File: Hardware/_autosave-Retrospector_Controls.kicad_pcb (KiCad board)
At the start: 2 copper layers, 60 x 110 mm, 32 parts, among them J1 Conn_01x08_Female, J10 Feedback_CV, J11 Audio_In_R, J12 Audio_Out_R, J13 Audio_Out_L, J14 Filter, J2 Conn_01x08_Female, J3 Conn_01x08_Female, J4 Conn_01x08_Female, J5 Audio_In_L, J6 Delay_CV_L, J7 Mix_CV, J8 Delay_CV_R, J9 Clock, U1 TB62781FNG

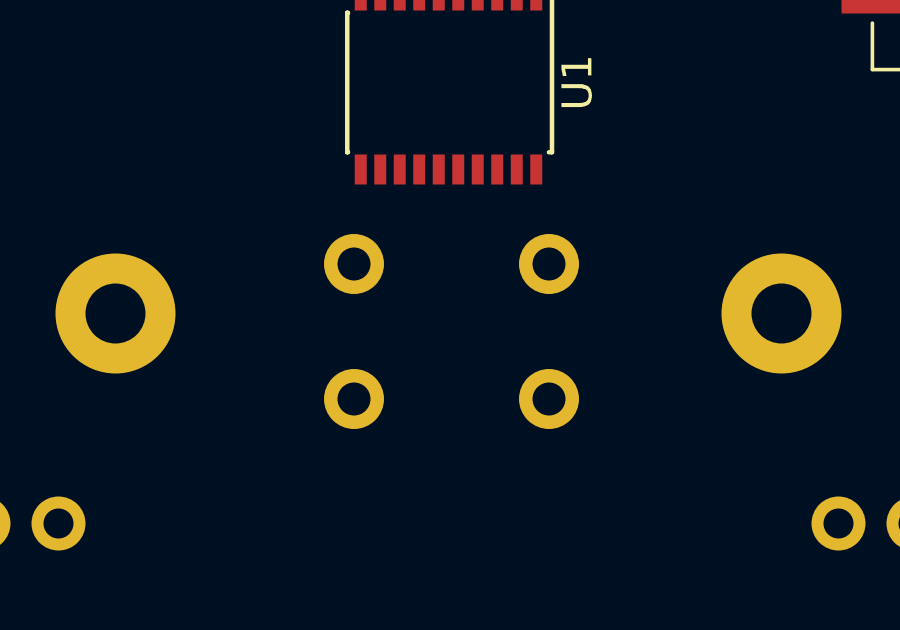
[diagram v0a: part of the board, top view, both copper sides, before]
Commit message: Final LED testing - decided on using Toshiba controller as WS2812B approach is very hacky and power inefficient
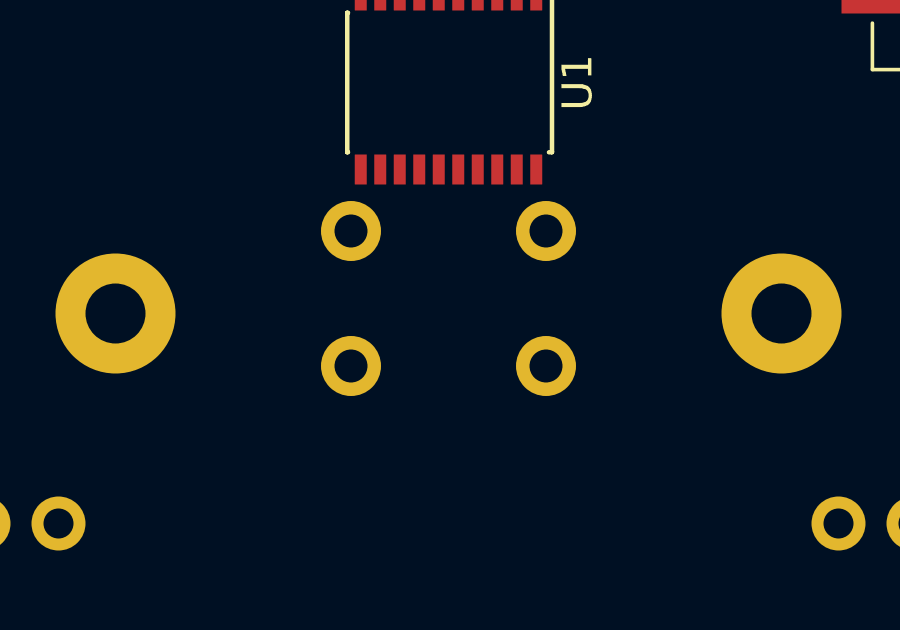
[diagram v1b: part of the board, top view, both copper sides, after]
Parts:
- moved LOCK1 1.10 mm to (130.0, 64.5)
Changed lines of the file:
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@@
   )
   (module Custom_Footprints:SW_PUSH_6mm_aligned (layer B.Cu)
-    (at 130.1 65.6)
+    (at 130 64.5)
     (descr https://www.omron.com/ecb/products/pdf/en-b3f.pdf)
     (tags "tact sw push 6mm")
